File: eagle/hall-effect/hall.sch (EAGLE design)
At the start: 3 parts, among them IC1 A1202LH

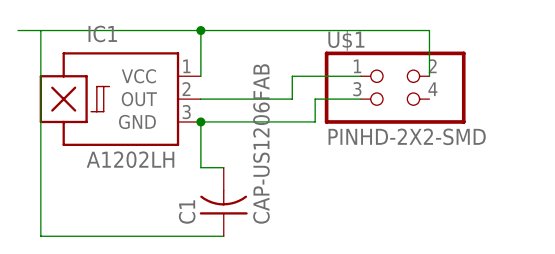
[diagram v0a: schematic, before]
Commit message: Hall Effect board uses through-hole cables instead of header pins
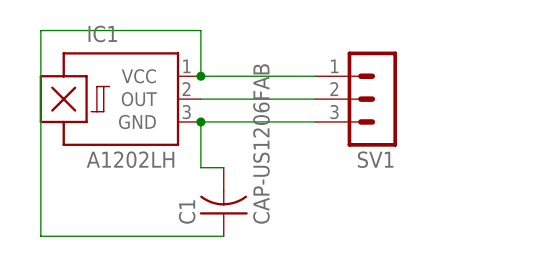
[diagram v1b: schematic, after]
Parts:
- removed U$1: PINHD-2X2-SMD, fab:PINHD-2X2-SMD
- added SV1: (no value), con-lstb:MA03-1
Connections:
- net N$1: now also SV1.1; no longer U$1.2
- net N$2: now also SV1.2; no longer U$1.1
- net N$3: now also SV1.3; no longer U$1.3
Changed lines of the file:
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@@
 <parts>
 <part name="IC1" library="allegro" deviceset="A12*?" device="LH" technology="02"/>
-<part name="U$1" library="fab" deviceset="PINHD-2X2-SMD" device=""/>
 <part name="C1" library="fab" deviceset="CAP-US" device="1206FAB"/>
+<part name="SV1" library="con-lstb" deviceset="MA03-1" device=""/>
 </parts>
 <sheets>
@@
 <instances>
 <instance part="IC1" gate="G$1" x="-2.54" y="55.88"/>
-<instance part="U$1" gate="G$1" x="27.94" y="55.88"/>
 <instance part="C1" gate="G$1" x="7.62" y="43.18" rot="R90"/>
+<instance part="SV1" gate="G$1" x="25.4" y="55.88" rot="R180"/>
 </instances>
 <busses>
@@
 <pinref part="IC1" gate="G$1" pin="VCC"/>
 <wire x1="5.08" y1="58.42" x2="5.08" y2="63.5" width="0.1524" layer="91"/>
-<wire x1="5.08" y1="63.5" x2="30.48" y2="63.5" width="0.1524" layer="91"/>
-<pinref part="U$1" gate="G$1" pin="2"/>
-<wire x1="30.48" y1="63.5" x2="30.48" y2="58.42" width="0.1524" layer="91"/>
 <wire x1="5.08" y1="63.5" x2="-12.7" y2="63.5" width="0.1524" layer="91"/>
-<junction x="5.08" y="63.5"/>
-<wire x1="-15.24" y1="63.5" x2="-12.7" y2="63.5" width="0.1524" layer="91"/>
 <wire x1="-12.7" y1="63.5" x2="-12.7" y2="40.64" width="0.1524" layer="91"/>
 <pinref part="C1" gate="G$1" pin="1"/>
 <wire x1="-12.7" y1="40.64" x2="7.62" y2="40.64" width="0.1524" layer="91"/>
+<pinref part="SV1" gate="G$1" pin="1"/>
+<wire x1="5.08" y1="58.42" x2="17.78" y2="58.42" width="0.1524" layer="91"/>
+<junction x="5.08" y="58.42"/>
 </segment>
 </net>
@@
 <segment>
 <pinref part="IC1" gate="G$1" pin="OUT"/>
-<wire x1="5.08" y1="55.88" x2="15.24" y2="55.88" width="0.1524" layer="91"/>
-<wire x1="15.24" y1="55.88" x2="15.24" y2="58.42" width="0.1524" layer="91"/>
-<pinref part="U$1" gate="G$1" pin="1"/>
-<wire x1="15.24" y1="58.42" x2="22.86" y2="58.42" width="0.1524" layer="91"/>
+<wire x1="5.08" y1="55.88" x2="17.78" y2="55.88" width="0.1524" layer="91"/>
+<pinref part="SV1" gate="G$1" pin="2"/>
 </segment>
 </net>
@@
 <pinref part="IC1" gate="G$1" pin="GND"/>
 <wire x1="5.08" y1="53.34" x2="17.78" y2="53.34" width="0.1524" layer="91"/>
-<wire x1="17.78" y1="53.34" x2="17.78" y2="55.88" width="0.1524" layer="91"/>
-<pinref part="U$1" gate="G$1" pin="3"/>
-<wire x1="17.78" y1="55.88" x2="22.86" y2="55.88" width="0.1524" layer="91"/>
 <wire x1="5.08" y1="53.34" x2="5.08" y2="48.26" width="0.1524" layer="91"/>
 <junction x="5.08" y="53.34"/>
 <pinref part="C1" gate="G$1" pin="2"/>
 <wire x1="5.08" y1="48.26" x2="7.62" y2="48.26" width="0.1524" layer="91"/>
+<pinref part="SV1" gate="G$1" pin="3"/>
 </segment>
 </net>
